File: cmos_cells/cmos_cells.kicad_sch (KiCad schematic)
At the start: 369 parts, among them P1 PMOS, P10 PMOS, P11 PMOS, P12 PMOS, P13 PMOS, P2 PMOS, P3 PMOS, P4 PMOS, P5 PMOS, P6 PMOS, P7 PMOS, P8 PMOS, P9 PMOS

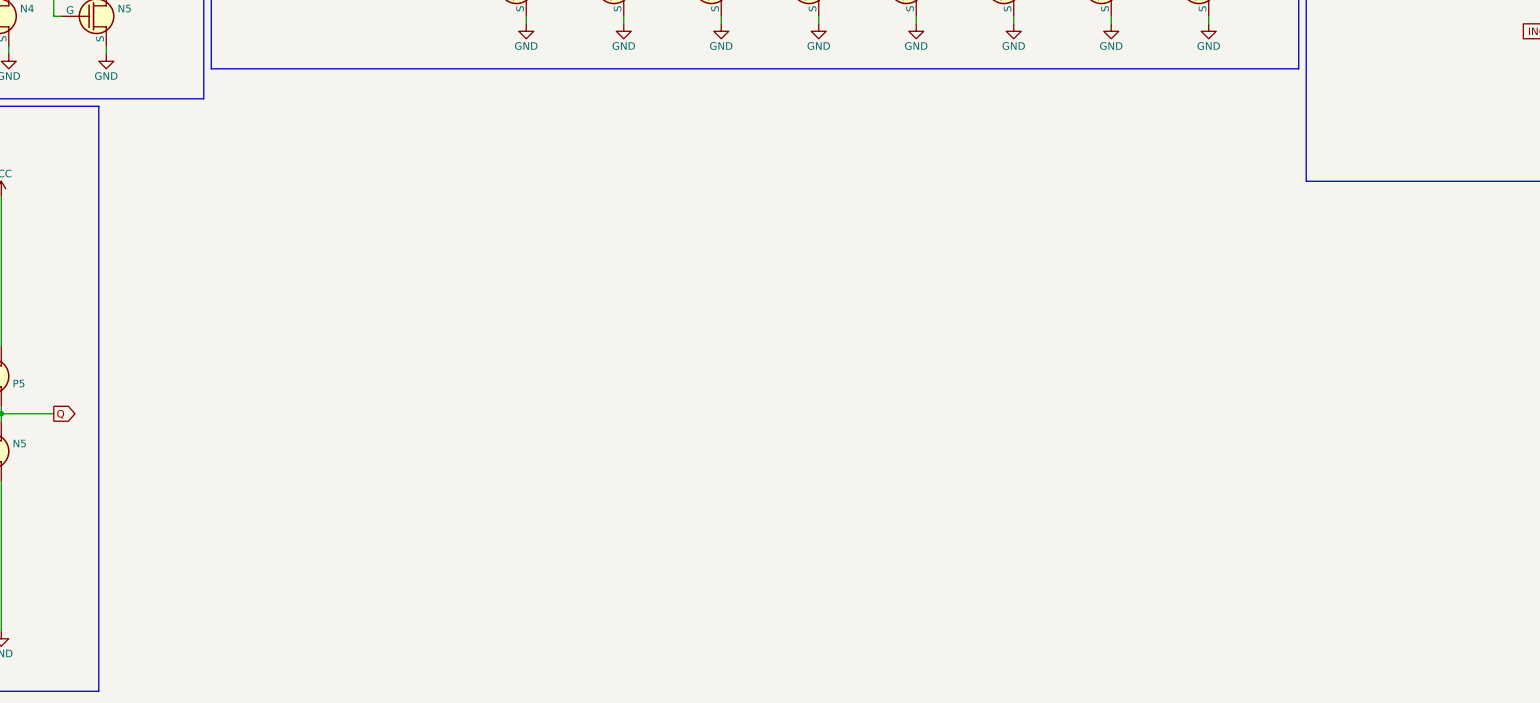
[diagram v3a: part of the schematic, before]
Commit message: Add schematic and layout for TRI_INV cells
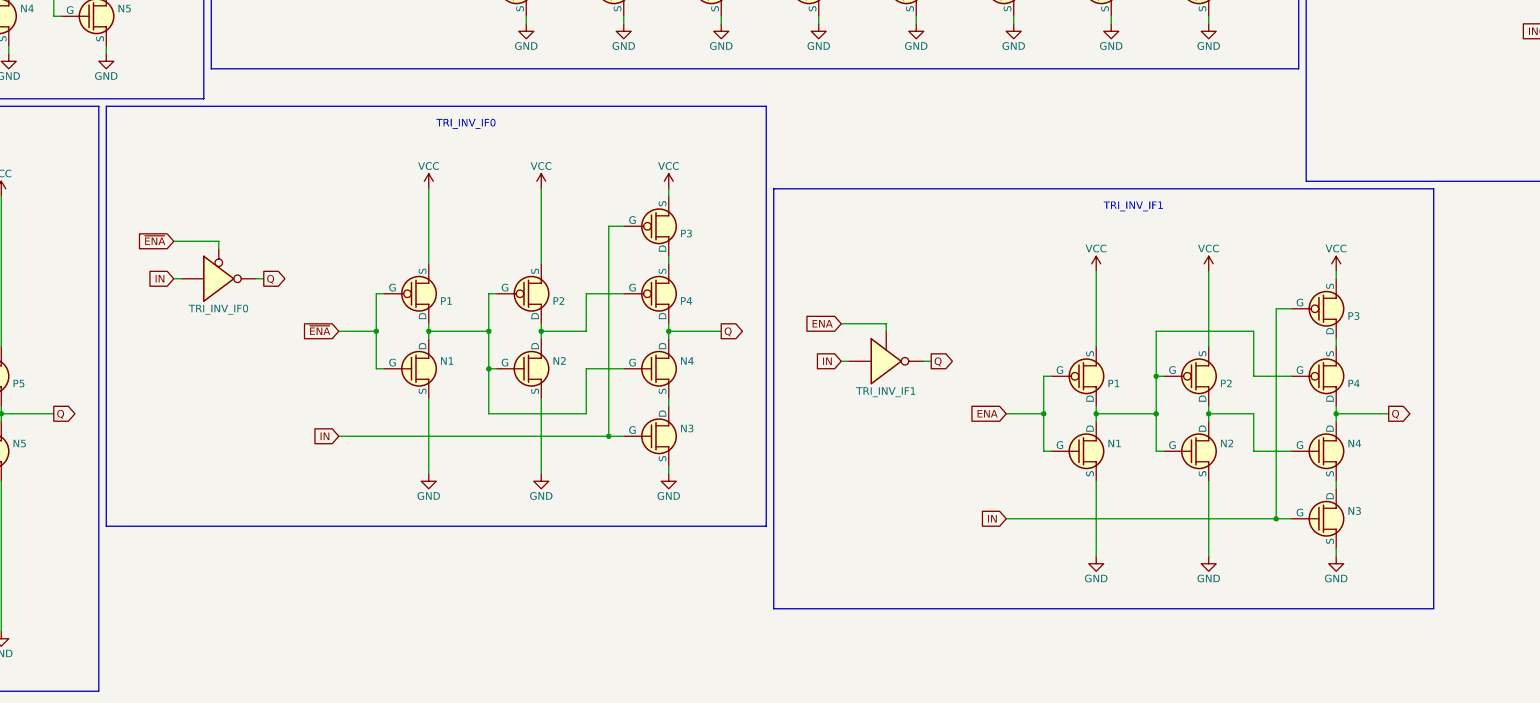
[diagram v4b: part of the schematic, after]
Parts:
- added N1 (x2), N2 (x2), N3 (x2), N4 (x2): NMOS, symbol DMG_CPU_Cells:NMOS
- added P1 (x2), P2 (x2), P3 (x2), P4 (x2): PMOS, symbol DMG_CPU_Cells:PMOS
- added U?: TRI_INV_IF0, symbol DMG_CPU_Cells:TRI_INV_IF0
- added U?: TRI_INV_IF1, symbol DMG_CPU_Cells:TRI_INV_IF1
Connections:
- net GND: now also N1.3 (S), N1.3 (S), N2.3 (S), N2.3 (S), N3.3 (S), N3.3 (S)
- net IN: now also N3.2 (G), N3.2 (G), P3.2 (G), P3.2 (G), U?.2, U?.2
- net Q: now also N4.1 (D), N4.1 (D), P4.1 (D), P4.1 (D), U?.3, U?.3
- net VCC: now also P1.3 (S), P1.3 (S), P2.3 (S), P2.3 (S), P3.3 (S), P3.3 (S)
- new net: N1.1 (D), N2.2 (G), P1.1 (D), P2.2 (G), P4.2 (G)
- new net: P3.1 (D), P4.3 (S) (x2)
- new net: N1.1 (D), N2.2 (G), N4.2 (G), P1.1 (D), P2.2 (G)
- new net: N2.1 (D), P2.1 (D), P4.2 (G)
- new net: N2.1 (D), N4.2 (G), P2.1 (D)
- new net: N3.1 (D), N4.3 (S) (x2)
- new net ENA: N1.2 (G), P1.2 (G), U?.1 (ENA)
- new net ~{ENA}: N1.2 (G), P1.2 (G), U?.1 (~{ENA})
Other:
- note added: "TRI_INV_IF0"
- note added: "TRI_INV_IF1"

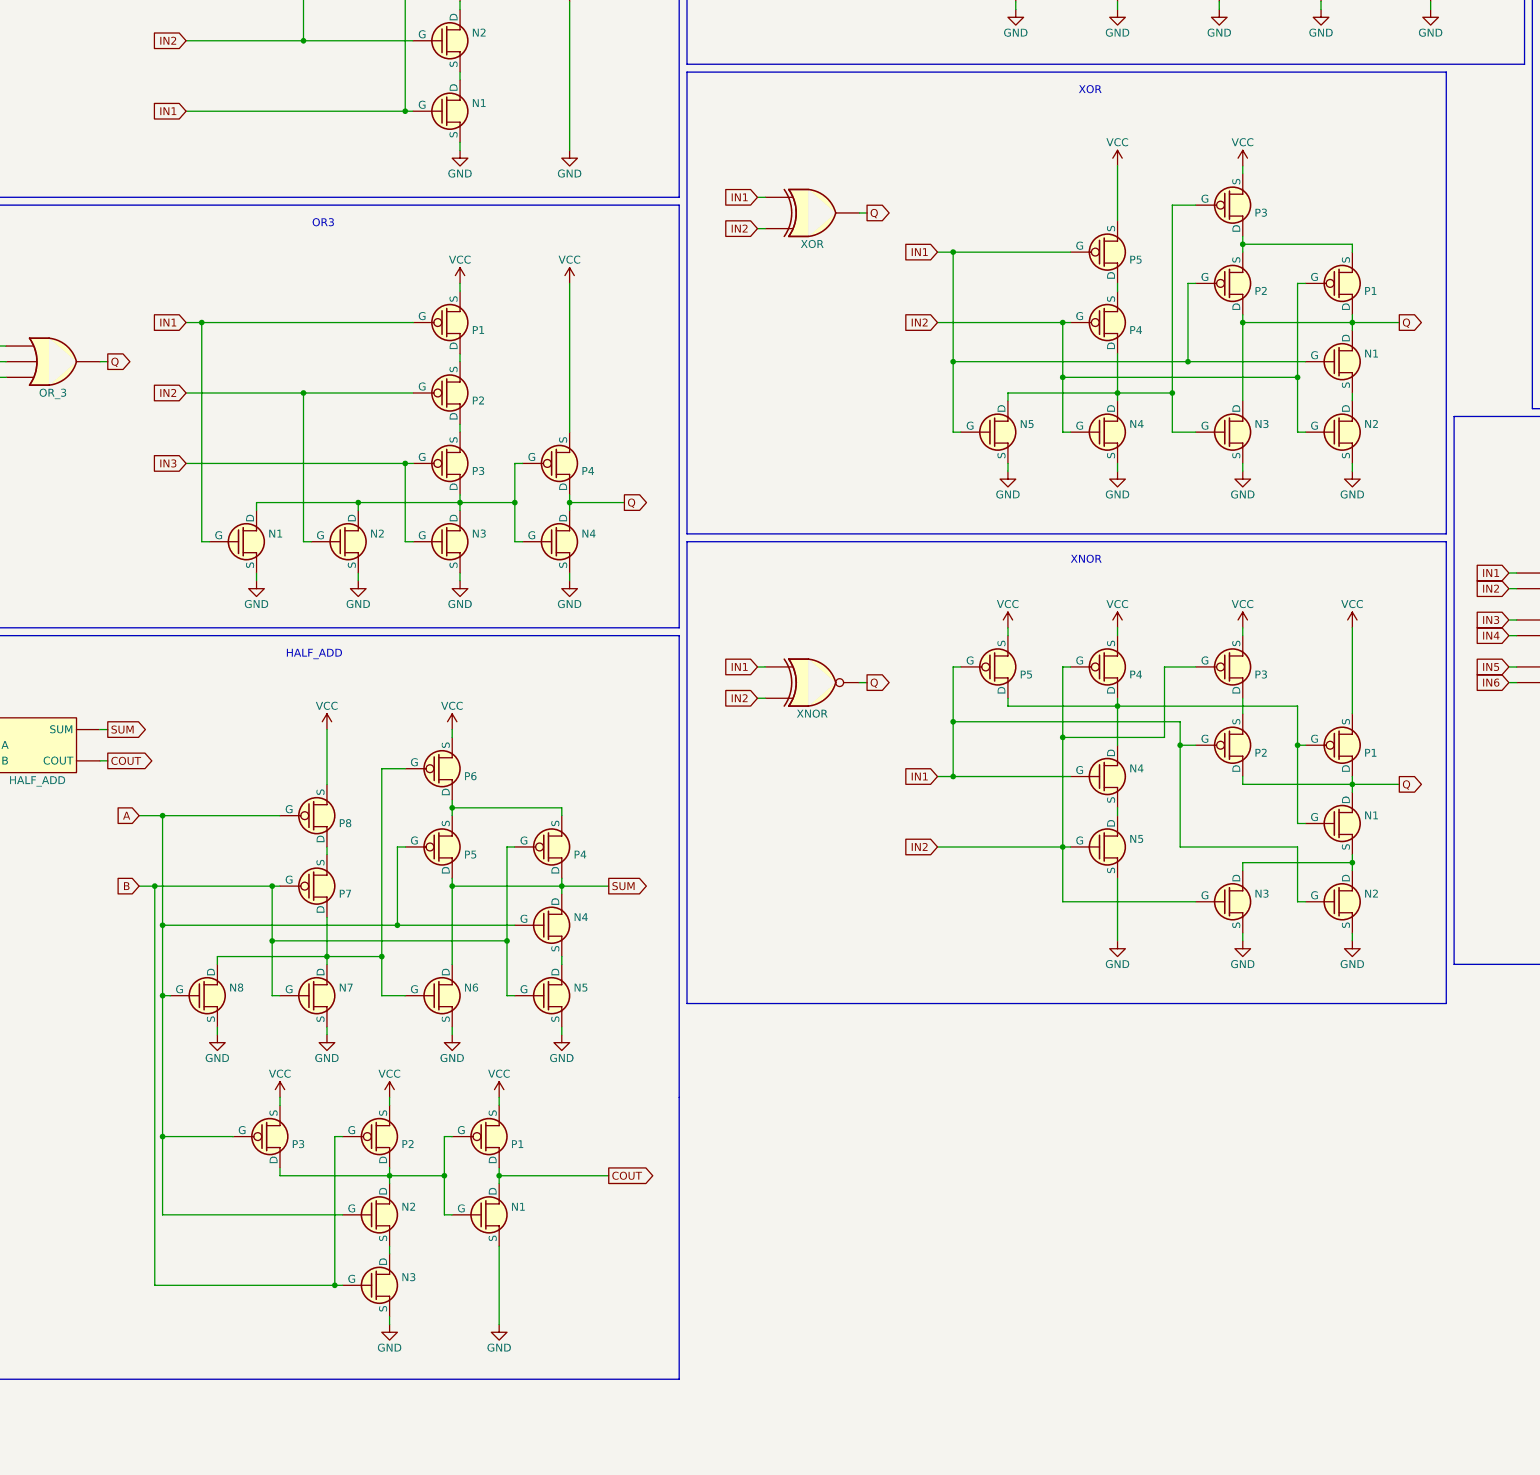
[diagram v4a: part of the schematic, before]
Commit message: Add XOR and XNOR layouts
and fix their schematics.
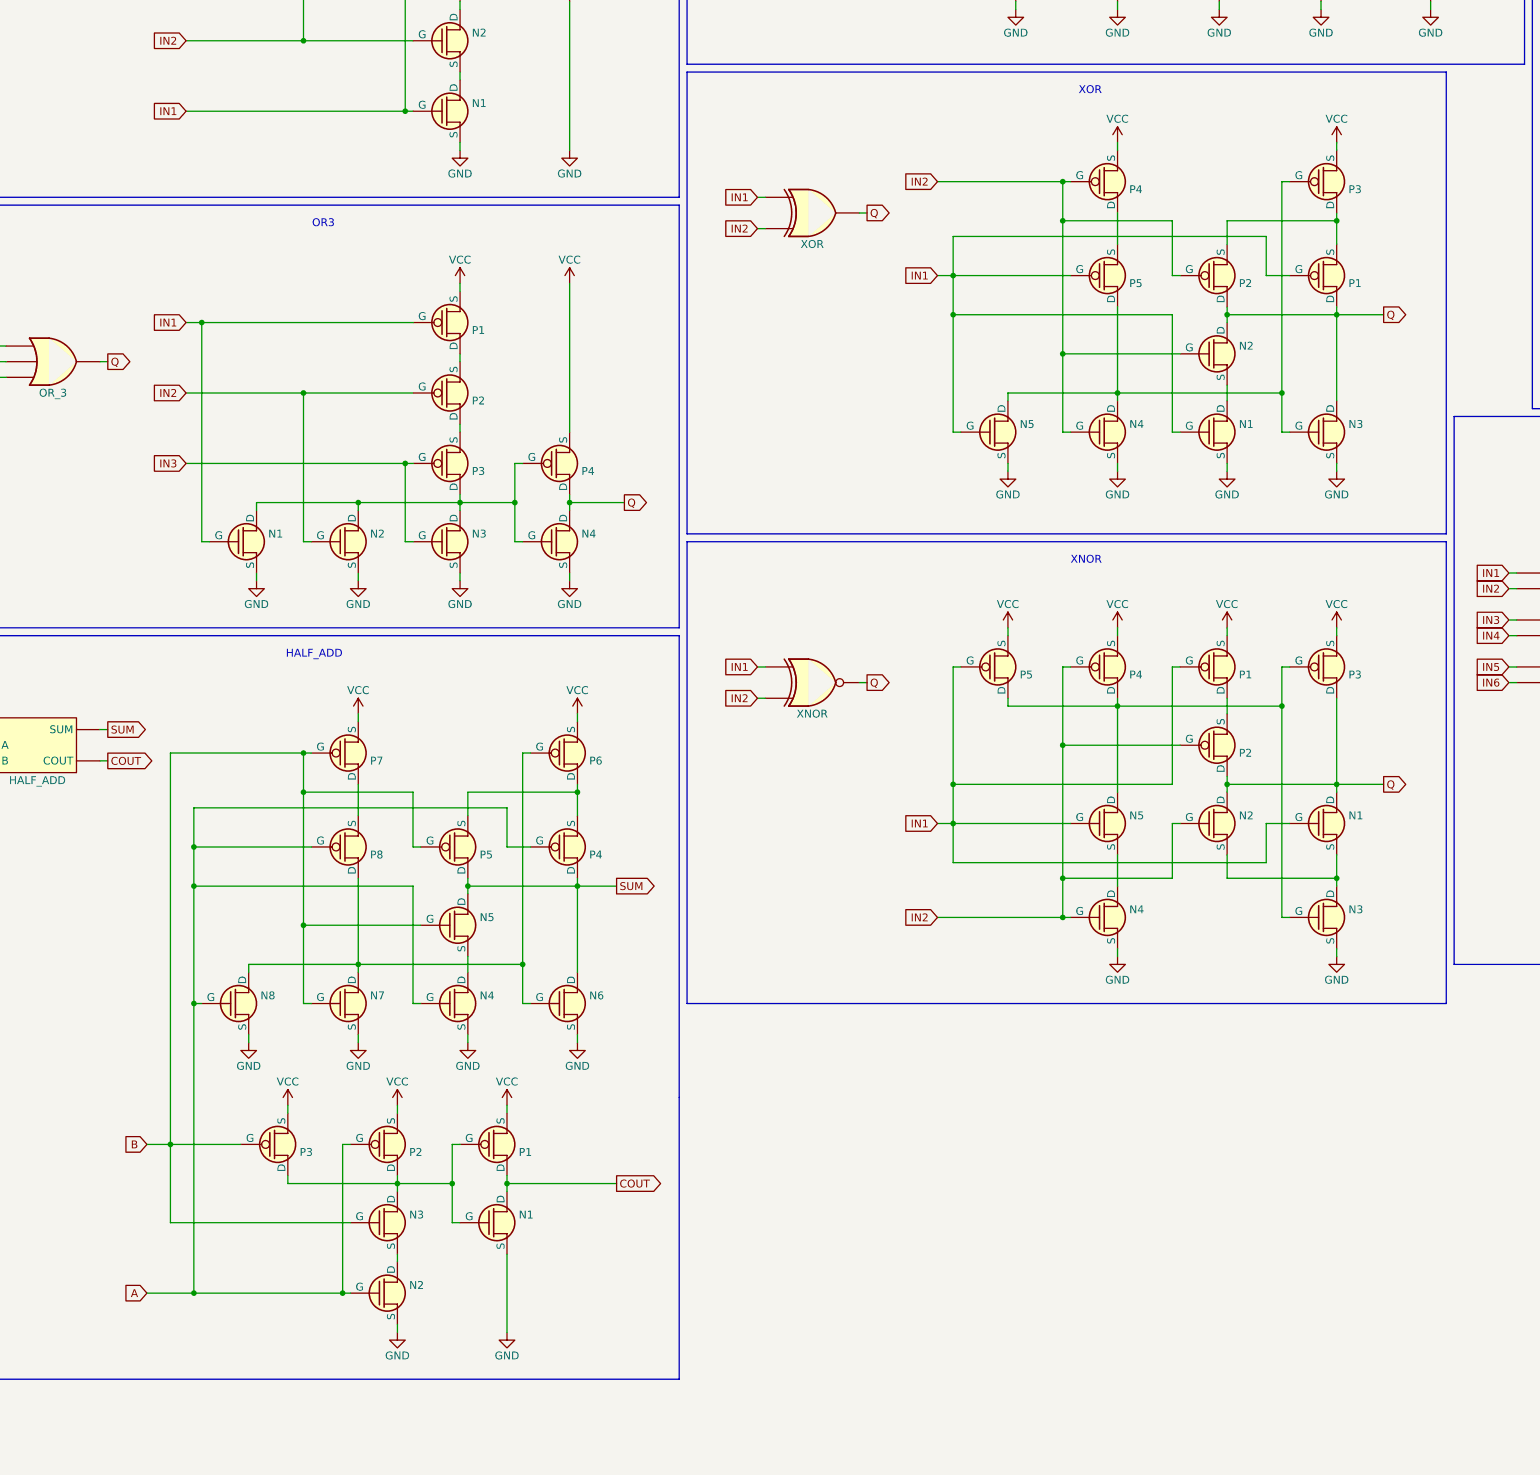
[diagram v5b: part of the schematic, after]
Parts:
- renumbered N3 to N1, N3 to N2, N1 to N2, N2 to N3, N5 to N4, N4 to N5, P3 to P1, P1 to P3, P5 to P4, P4 to P5
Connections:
- net A: now also N2.2 (G), P2.2 (G), P4.2 (G); no longer N3.2 (G), P3.2 (G), P5.2 (G)
- net B: now also N3.2 (G), P3.2 (G), P5.2 (G); no longer N2.2 (G), P2.2 (G), P4.2 (G)
- net GND: now also N4.3 (S); no longer N2.3 (S), N5.3 (S)
- net IN1: now also N1.2 (G), N1.2 (G), P1.2 (G), P1.2 (G), P5.2 (G); no longer N2.2 (G), N2.2 (G), P2.2 (G), P2.2 (G), P4.2 (G)
- net IN2: now also N2.2 (G), N2.2 (G), P2.2 (G), P2.2 (G), P4.2 (G); no longer N3.2 (G), N3.2 (G), P1.2 (G), P1.2 (G), P5.2 (G)
- net Q: now also N2.1 (D), N3.1 (D); no longer N1.1 (D)
- net SUM: now also N5.1 (D); no longer N4.1 (D)
- net VCC: now also P7.3 (S); no longer P8.3 (S)
- net at P8.1 (D): now also N6.2 (G), N7.1 (D), N8.1 (D), P6.2 (G); no longer P7.3 (S)
- net at N4.1 (D), N5.1 (D), P3.2 (G)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: now also N3.2 (G); no longer N1.2 (G)
- net at N5.1 (D), P3.2 (G), P4.1 (D)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: now also N3.2 (G); no longer N1.2 (G)
- net at N2.3 (S): now also N1.1 (D); no longer N3.1 (D)
- net at N1.3 (S), N3.1 (D): now also N2.3 (S); no longer N2.1 (D)
- new net: N4.1 (D), N5.3 (S)
- new net: P7.1 (D), P8.3 (S)
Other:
- moved on the sheet: N1, N2, N3, N4, N5, P1, P2, P3, P4, P5

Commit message: Add layout and schematics for D-Latches, AO3 and SUPPLY cells
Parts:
- removed P1: PMOS, symbol DMG_CPU_Cells:PMOS
- added N1 (x3), N2 (x3), N3 (x3), N4 (x3), N5 (x3), N6 (x3), N7 (x2), N8: NMOS, symbol DMG_CPU_Cells:NMOS
- added P1 (x4), P2 (x3), P3 (x3), P4 (x3), P5 (x3), P6 (x3), P7 (x2), P8: PMOS, symbol DMG_CPU_Cells:PMOS
- added U?: D_LATCH_A, symbol DMG_CPU_Cells:D_LATCH_A
- added U?: D_LATCH_A2, symbol DMG_CPU_Cells:D_LATCH_A2
- added U? (x11): INVERTER_A, symbol DMG_CPU_Cells:INVERTER_A
- added U? (x3): MUX, symbol DMG_CPU_Cells:MUX
- added U?: D_LATCH_B, symbol DMG_CPU_Cells:D_LATCH_B
- added U?: NAND_2, symbol DMG_CPU_Cells:NAND_2
- added U?: DR_LATCH, symbol DMG_CPU_Cells:DR_LATCH
- renumbered P11 to P10, P6 to P11, P3 to P2, P5 to P2, P7 to P2, P4 to P2, P2 to P3, P5 to P4, P6 to P4, P8 to P4, P3 to P5, P7 to P6, P9 to P6, P4 to P7, P10 to P8, P5 to P9
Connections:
- net ENA: now also N1.2 (G), N1.2 (G), N1.2 (G), P1.2 (G), P2.2 (G), P2.2 (G), U?.1, U?.1, U?.1, U?.1 (ENA), U?.1 (~{ENA}), U?.1 (~{ENA}), U?.1 (~{ENA}), U?.3 (ENA), U?.3 (ENA), U?.3 (ENA)
- net GND: now also N1.3 (S), N3.3 (S), N3.3 (S), N4.3 (S), N4.3 (S), N5.3 (S), N5.3 (S), N5.3 (S), N6.3 (S), N6.3 (S), N6.3 (S), N7.3 (S), N7.3 (S), N8.3 (S)
- net Q: now also N5.1 (D), N6.1 (D), N7.1 (D), P5.1 (D), P6.1 (D), P7.1 (D), U?.2, U?.2, U?.2, U?.3 (Q), U?.4 (Q), U?.4 (Q), U?.5 (Q)
- net VCC: now also P1.3 (S), P1.3 (S), P3.3 (S), P3.3 (S), P4.3 (S), P4.3 (S), P4.3 (S), P5.3 (S), P5.3 (S), P5.3 (S), P6.3 (S), P6.3 (S), P6.3 (S), P7.3 (S), P7.3 (S), P8.3 (S)
- net ~{ENA}: now also N2.2 (G), N2.2 (G), P1.2 (G), P1.2 (G), P1.2 (G)
- net at N1.1 (D), N2.2 (G), N4.2 (G)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: now also P1.1 (D)
- new net: N1.1 (D), N2.1 (D), N3.2 (G), P1.1 (D), P2.1 (D), P3.2 (G)
- new net: N5.1 (D), N6.2 (G), N7.2 (G), P5.1 (D), P6.2 (G), P7.2 (G)
- new net: N2.1 (D), N3.1 (D), N5.2 (G), P2.1 (D), P3.1 (D), P5.2 (G)
- new net: N4.1 (D), N5.2 (G), N6.2 (G), P3.1 (D), P4.1 (D), P5.2 (G), P6.2 (G)
- new net: N1.1 (D), N2.1 (D), N4.2 (G), P1.1 (D), P2.1 (D), P4.2 (G)
- new net: U?.1, U?.1, U?.3
- new net: N2.3 (S), N4.1 (D), N6.2 (G), P2.3 (S), P4.1 (D), P6.2 (G)
- new net: N3.3 (S), N6.1 (D), N8.2 (G), P3.3 (S), P6.1 (D), P8.2 (G)
- new net: U?.1, U?.4 (x3)
- new net: U?.1, U?.1, U?.2 (x2)
- new net: N3.1 (D), N4.2 (G), N5.2 (G), P3.1 (D), P4.2 (G), P5.2 (G)
- new net: U?.1, U?.2, U?.3 (x3)
- new net: N2.3 (S), N5.1 (D), N7.2 (G), P2.3 (S), P5.1 (D), P7.2 (G)
- new net: N2.2 (G), N4.1 (D), P3.2 (G), P4.1 (D)
- new net: N1.1 (D), N3.2 (G), N4.2 (G), P1.1 (D), P2.2 (G), P4.2 (G)
- new net: N3.1 (D), N4.3 (S)
- new net D: N1.3 (S), N1.3 (S), N2.3 (S), P1.3 (S), P1.3 (S), P2.3 (S), U?.2, U?.2, U?.2, U?.2 (D), U?.2 (D), U?.2 (D), U?.2 (D)
- new net ~{Q}: N6.1 (D), N7.1 (D), N8.1 (D), P6.1 (D), P7.1 (D), P8.1 (D), U?.2, U?.2, U?.2, U?.4 (~{Q}), U?.5 (~{Q}), U?.6 (~{Q})
- new net ~{RESET}: N3.2 (G), P3.2 (G), U?.2, U?.4 (~{RESET})
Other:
- note added: "DR_LATCH"
- note added: "D_LATCH - Variant A"
- note added: "D_LATCH - Variant B"
- note added: "SUPPLY"
